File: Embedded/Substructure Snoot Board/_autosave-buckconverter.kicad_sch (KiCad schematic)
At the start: 33 parts, among them U10 LM5176PWP

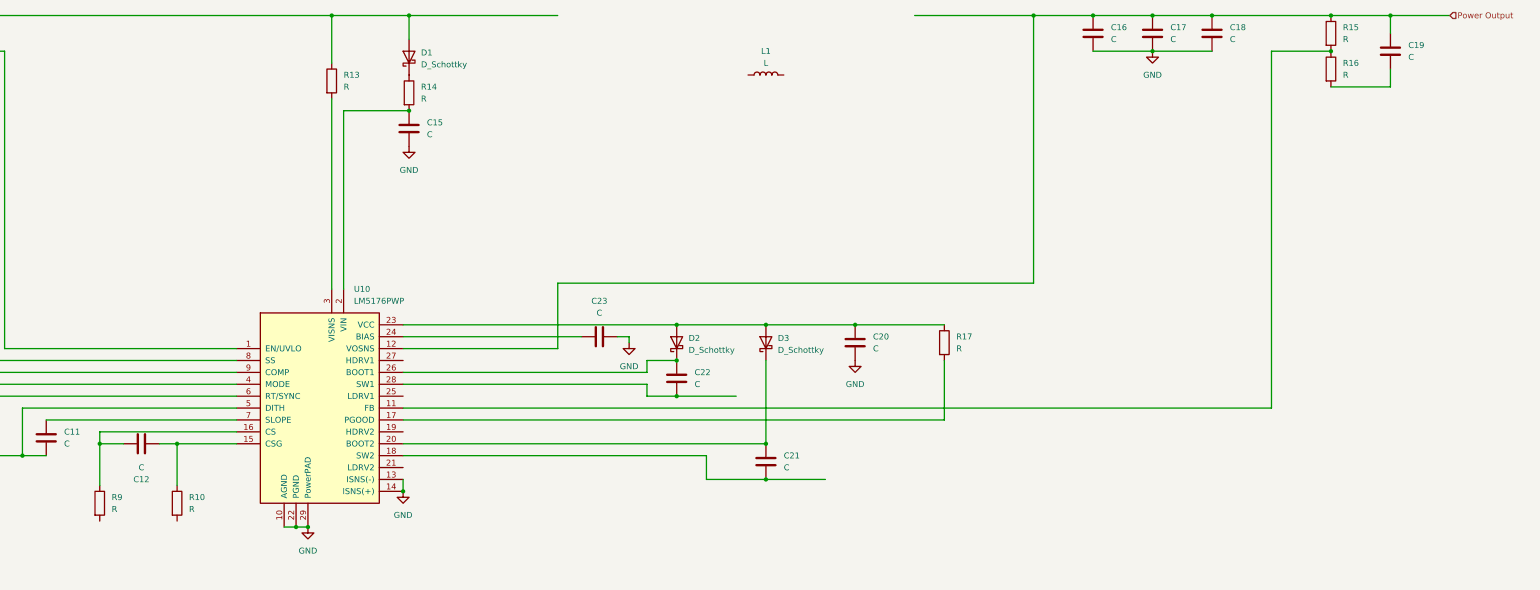
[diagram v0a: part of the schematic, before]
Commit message: Added Buck Converter Components
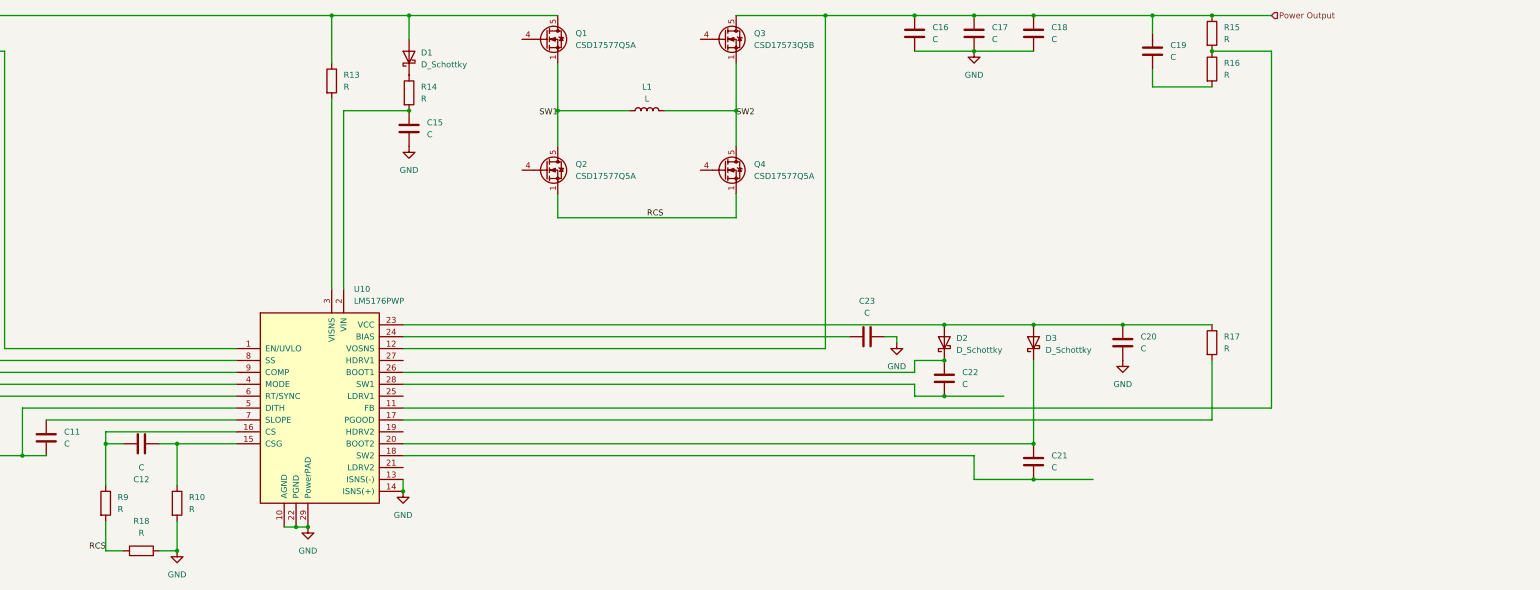
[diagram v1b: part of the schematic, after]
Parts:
- added Q1, Q2, Q4: CSD17577Q5A, Package_TO_SOT_SMD:TDSON-8-1, symbol Transistor_FET:CSD17577Q5A
- added Q3: CSD17573Q5B, Package_TO_SOT_SMD:TDSON-8-1, symbol Transistor_FET:CSD17573Q5B
- added R18: R, symbol Device:R
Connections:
- net GND: now also R10.2, R18.2
- net Power Input: now also Q1.5 (D)
- net Power Output: now also Q3.5 (D)
- net RCS: now reaches R9.2
- net RCS: now also Q2.1 (S), Q2.2 (S), Q2.3 (S), Q4.1 (S), Q4.2 (S), Q4.3 (S), R18.1
- net SW1: now reaches L1.1
- net SW1: now also Q1.1 (S), Q1.2 (S), Q1.3 (S), Q2.5 (D)
- net SW2: now reaches L1.2
- net SW2: now also Q3.1 (S), Q3.2 (S), Q3.3 (S), Q4.5 (D)
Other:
- moved on the sheet: C16, C17, C18, C19, C20, C21, C22, C23, D2, D3, L1, R15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
